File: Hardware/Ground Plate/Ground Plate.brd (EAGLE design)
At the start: 203.2 x 203.2 mm, 12 parts

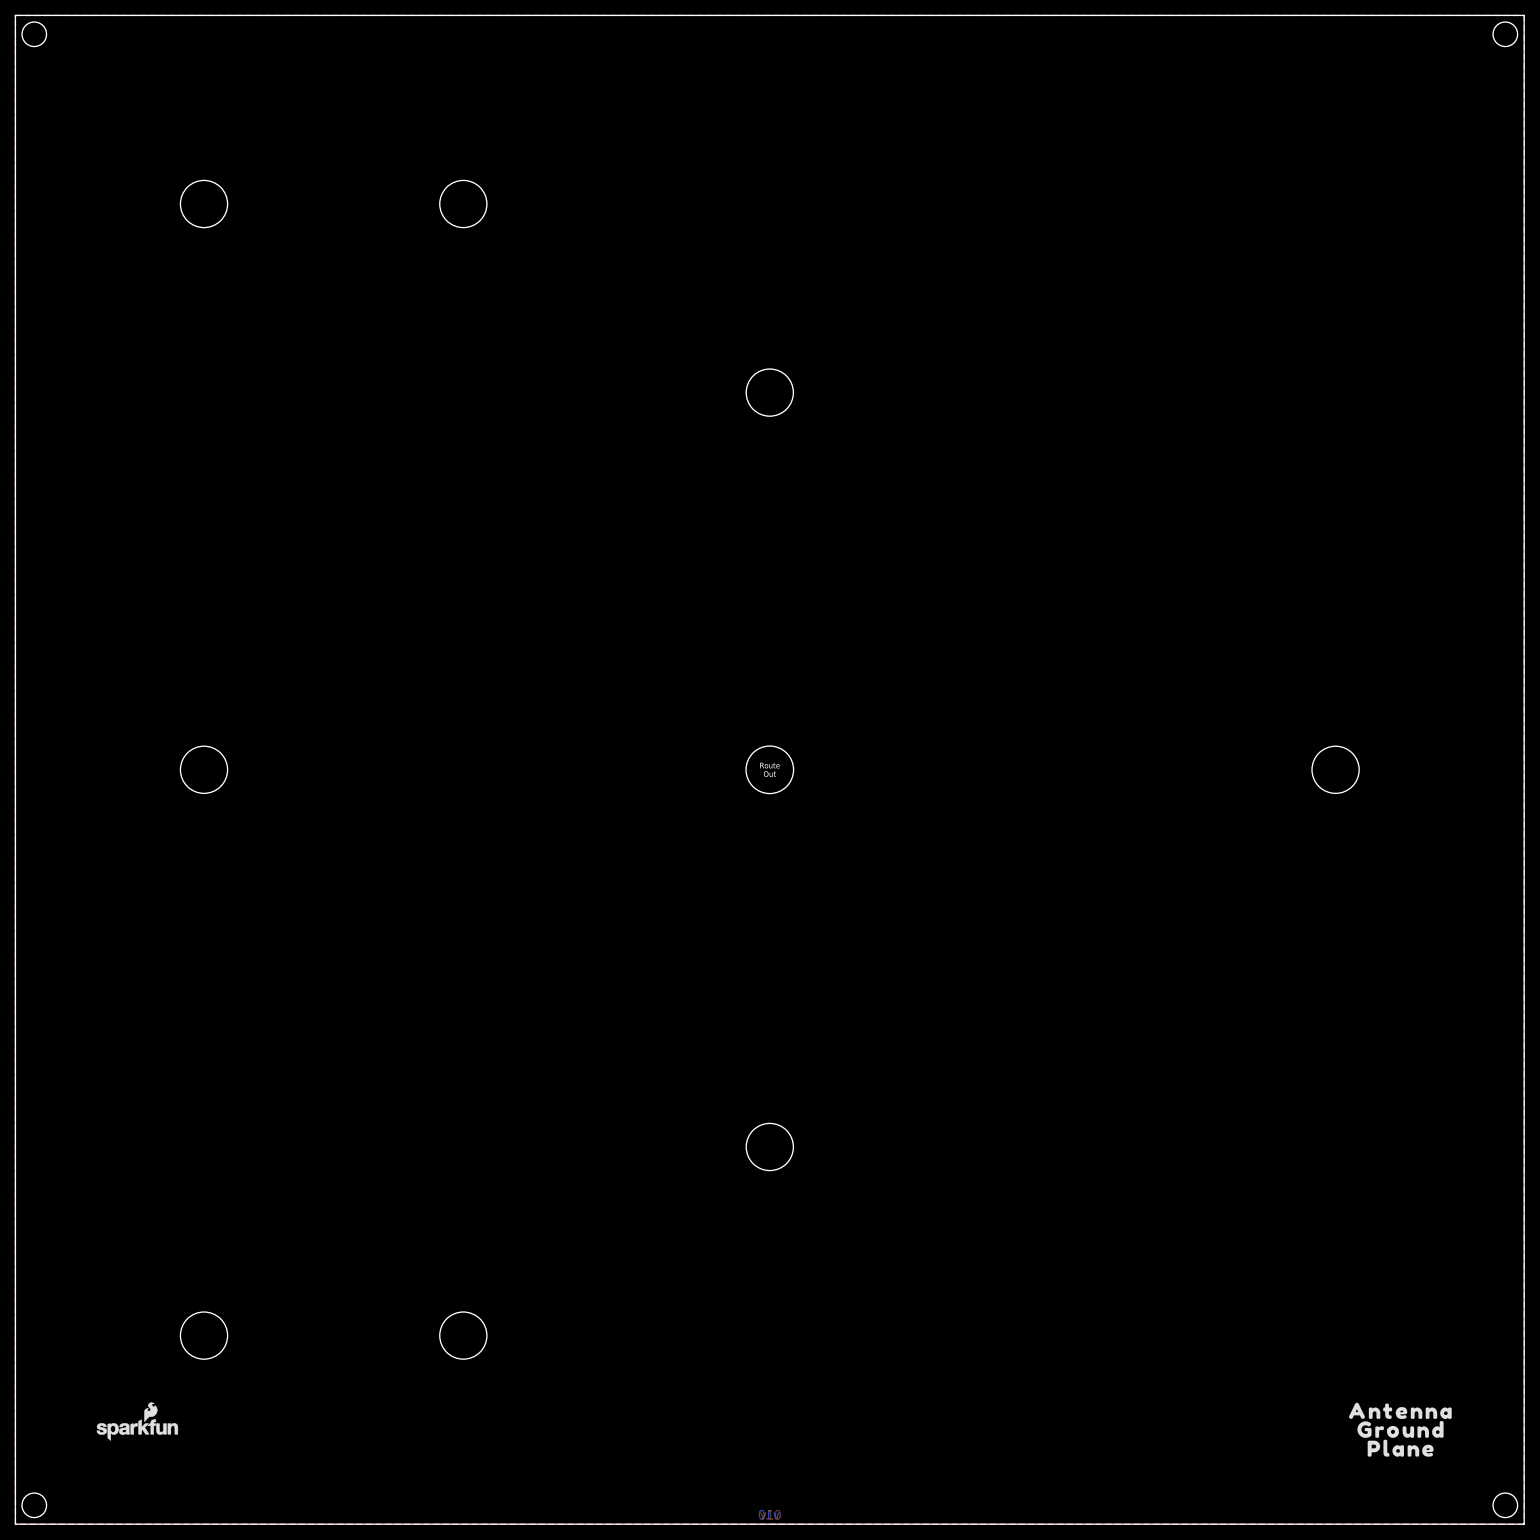
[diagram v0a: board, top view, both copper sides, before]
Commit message: Combining ground plate versions
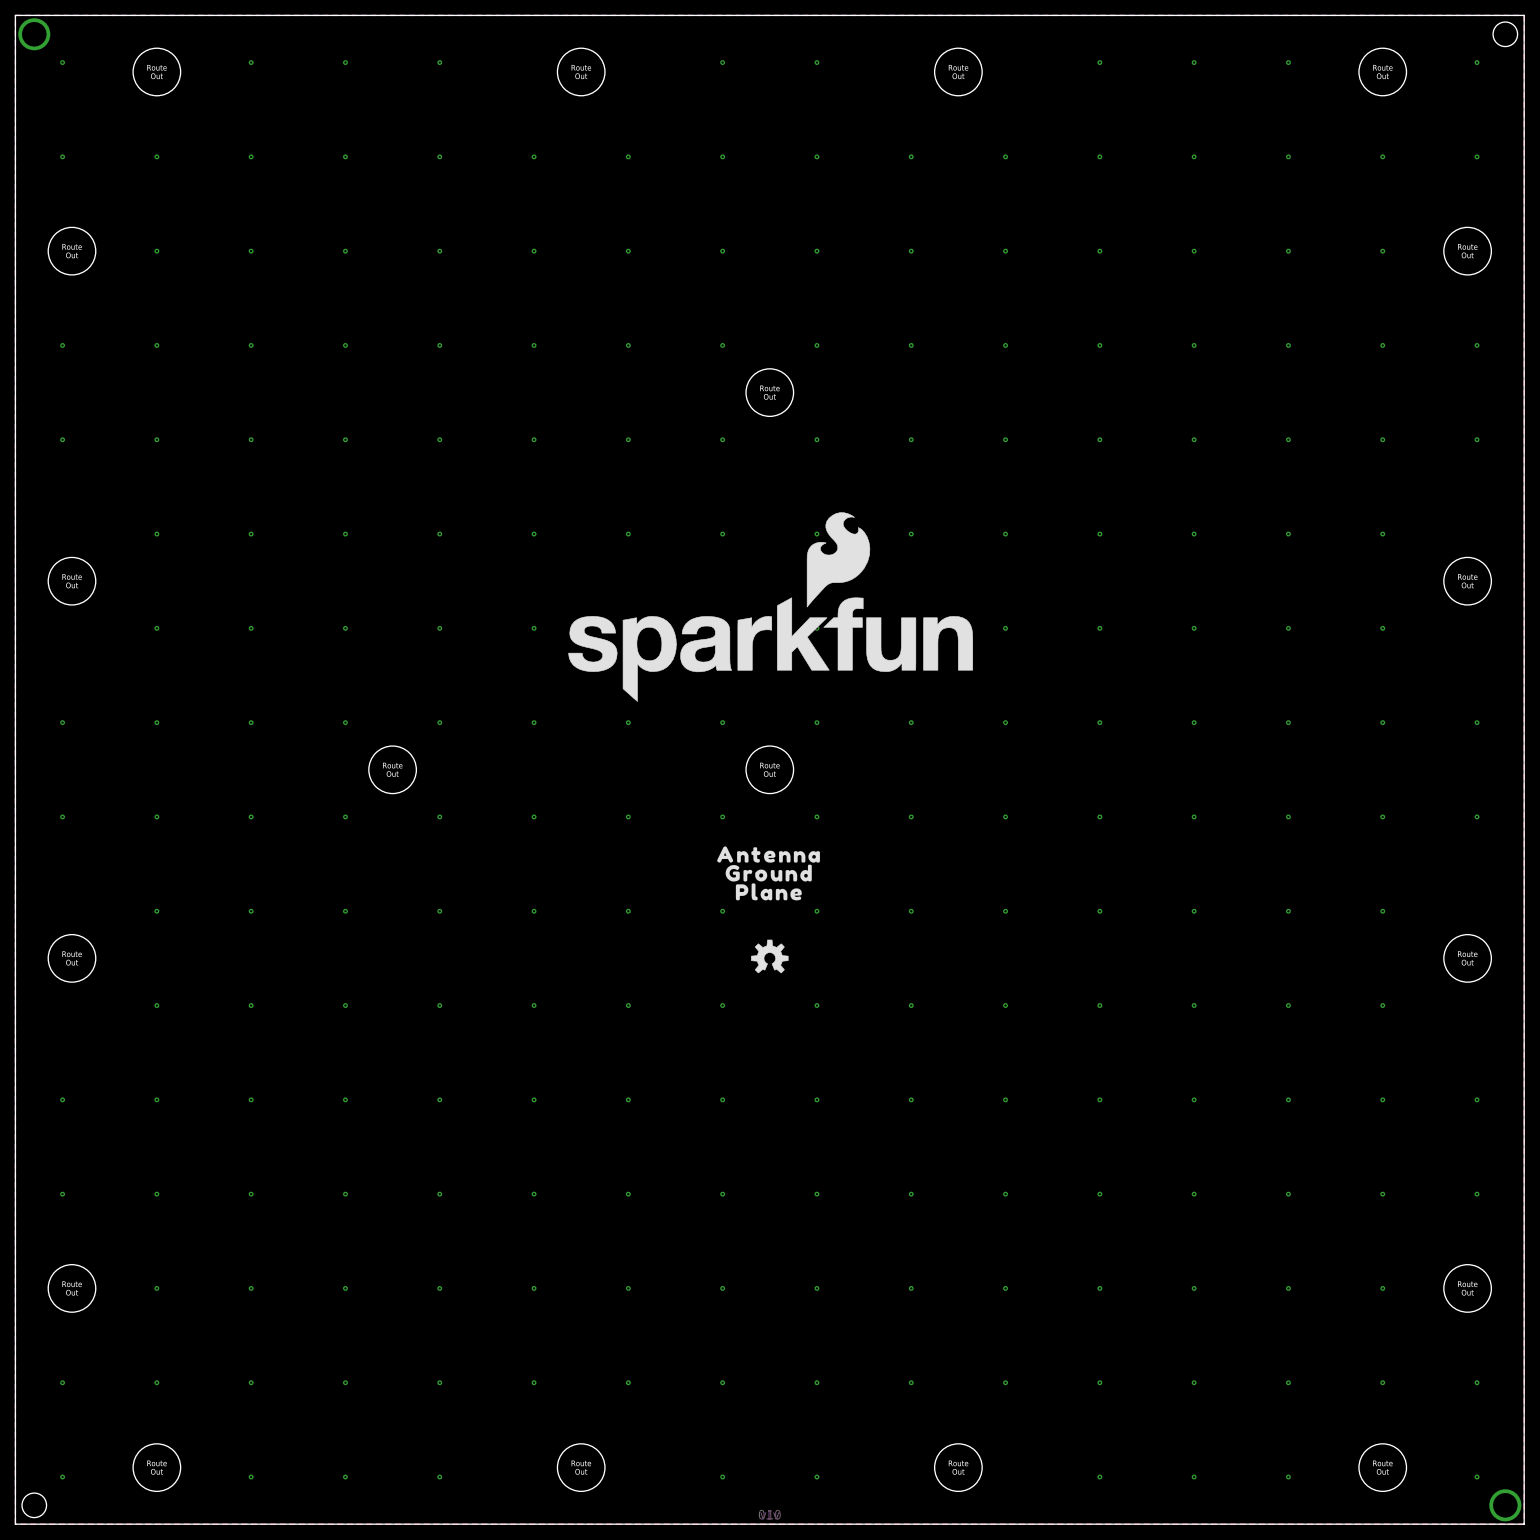
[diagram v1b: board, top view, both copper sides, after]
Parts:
- removed JP101, JP41: STAND-OFF, SparkFun:STAND-OFF
- added U$10, U$11, U$12, U$22, U$5, U$6, U$7, U$8, U$9: SMA-ANTENNA-THREADED-NOT-KEYED_WITH-STOP, SparkFun-Hardware:SMA-THREADED_WITH-STOP
- added U$13, U$14, U$15, U$16, U$17, U$18, U$19, U$20, U$21: SMA-ANTENNA-THREADED-NOT-KEYED_NO-COPPER, SparkFun-Hardware:SMA-THREADED_NO-COPPER
- LOGO1: value OSHW-LOGOMINI -> OSHW-LOGOM; device SparkFun-Aesthetics:OSHW-LOGO-MINI -> SparkFun-Aesthetics:OSHW-LOGO-M
- LOGO2: value SFE_LOGO_NAME_FLAME.1_INCH -> SFE_LOGO_NAME_FLAME.5_INCH; device SparkFun-Aesthetics:SFE_LOGO_NAME_FLAME_.1 -> SparkFun-Aesthetics:SFE_LOGO_NAME_FLAME_.5
- U$54: value SMA-ANTENNA-THREADED -> SMA-ANTENNA-THREADED-NOT-KEYED_WITH-STOP; device SparkFun-Hardware:SMA-THREADED -> SparkFun-Hardware:SMA-THREADED_WITH-STOP
- moved JP91 198.1 mm to (200.7, 200.7)
- moved LOGO1 119.9 mm to (101.6, 76.2), flipped to the top
- moved U$1 113.4 mm to (101.6, 90.2)
- moved U$3 113.4 mm to (101.6, 87.6)
- moved U$4 113.4 mm to (101.6, 85.1)
- moved LOGO2 113.3 mm to (73.7, 110.5)
- moved U$54 97.4 mm to (76.2, 7.62)
- moved FRAME1 84.1 mm to (248.9, 8.89)
